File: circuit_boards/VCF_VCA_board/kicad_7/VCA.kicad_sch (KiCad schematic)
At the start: 15 parts, among them U6 TL072, U7 TL072, U9 SSI2164

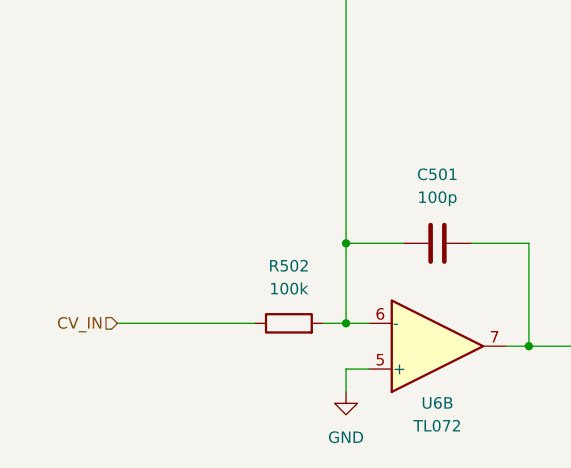
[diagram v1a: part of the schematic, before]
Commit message: Update PCBs, tweak vals, add VCF CV from DAC
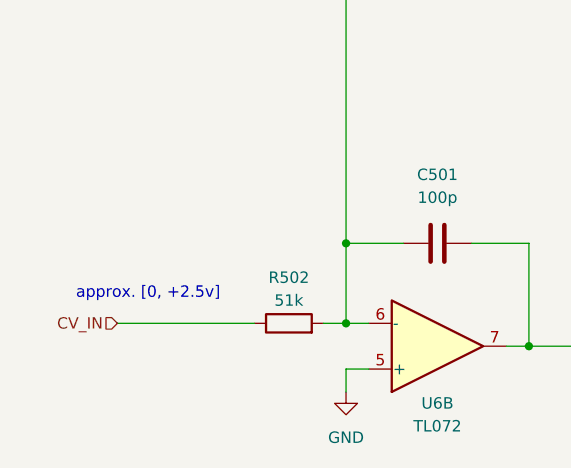
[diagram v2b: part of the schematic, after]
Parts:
- R502: value 100k -> 51k
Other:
- note added: "approx. [0, +2.5v]"
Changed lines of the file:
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@@
   (title_block
     (title "MICRO-OX VCF/VCA board")
-    (date "2023-04-13")
-    (rev "0")
+    (date "2023-04-25")
+    (rev "0.1")
     (comment 1 "creativecommons.org/licenses/by/4.0/")
     (comment 2 "License: CC by 4.0")
@@
   (wire (pts (xy 181.61 63.5) (xy 184.15 63.5))
     (stroke (width 0) (type default))
+  )
+  (text "approx. [0, +2.5v]" (at 72.39 146.05 0)
+    (effects (font (size 1.27 1.27)) (justify right bottom))
   )
   (global_label "-5V_REF" (shape input) (at 151.13 109.22 0) (fields_autoplaced)
@@
   (symbol (lib_id "Device:R") (at 80.01 148.59 90) (unit 1)
     (in_bom yes) (on_board yes) (dnp no) (fields_autoplaced)
-    (property "Reference" "R502" (at 80.01 142.24 90)
-      (effects (font (size 1.27 1.27)))
-    )
-    (property "Value" "100k" (at 80.01 144.78 90)
-      (effects (font (size 1.27 1.27)))
-    )
+    (property "Reference" "R502" (at 80.01 143.51 90)
+      (effects (font (size 1.27 1.27)))
+    )
+    (property "Value" "51k" (at 80.01 146.05 90)
+      (effects (font (size 1.27 1.27)))
+    )

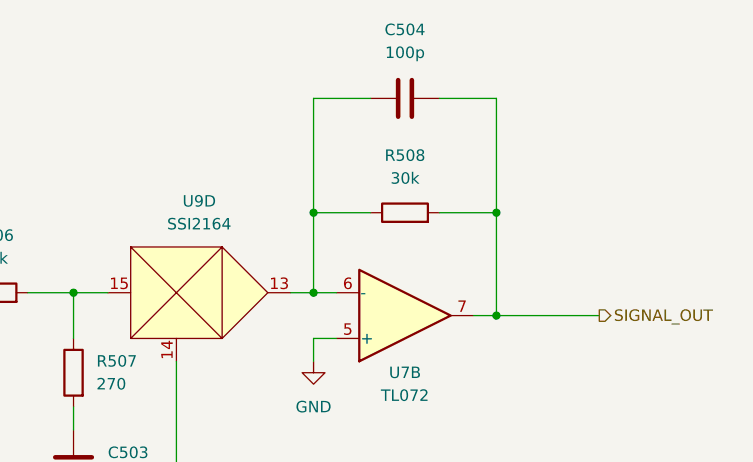
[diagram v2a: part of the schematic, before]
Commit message: Increase gain for hotter output
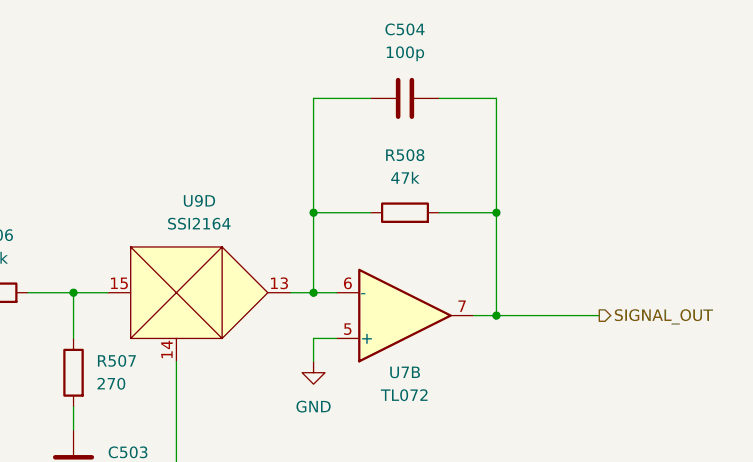
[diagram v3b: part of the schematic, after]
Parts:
- R508: value 30k -> 47k
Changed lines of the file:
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@@
       (effects (font (size 1.27 1.27)))
     )
-    (property "Value" "30k" (at 194.31 50.8 90)
+    (property "Value" "47k" (at 194.31 50.8 90)
       (effects (font (size 1.27 1.27)))
     )
